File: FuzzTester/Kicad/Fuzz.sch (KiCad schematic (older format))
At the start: 8 parts, among them J1 Audio In/Out JST XH, J2 POT B10K JST XH, J3 POT B5K JST XH, J4 VOL POT A100K JST XH

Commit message: PCB fixes
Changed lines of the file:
@@
 encoding utf-8
 Sheet 1 10
-Title ""
+Title "Guitar Pedal Effect Fuzz Digitally Controlled"
 Date ""
-Rev ""
+Rev "0.1"
 Comp ""
 Comment1 ""
@@
 U 1 1 5EC42733
 P 5600 2200
-F 0 "R2" V 5393 2200 50  0000 C CNN
-F 1 "100K" V 5484 2200 50  0000 C CNN
+F 0 "R2" V 5500 2200 50  0000 C CNN
+F 1 "100K" V 5600 2200 50  0000 C CNN
 F 2 "Resistor_SMD:R_0805_2012Metric_Pad1.15x1.40mm_HandSolder" V 5530 2200 50  0001 C CNN
 F 3 "~" H 5600 2200 50  0001 C CNN
@@
 P 8400 1450
 F 0 "R3" H 8470 1496 50  0000 L CNN
-F 1 "10K" H 8470 1405 50  0000 L CNN
+F 1 "10K" H 8450 1400 50  0000 L CNN
 F 2 "Resistor_SMD:R_0805_2012Metric_Pad1.15x1.40mm_HandSolder" V 8330 1450 50  0001 C CNN
 F 3 "~" H 8400 1450 50  0001 C CNN

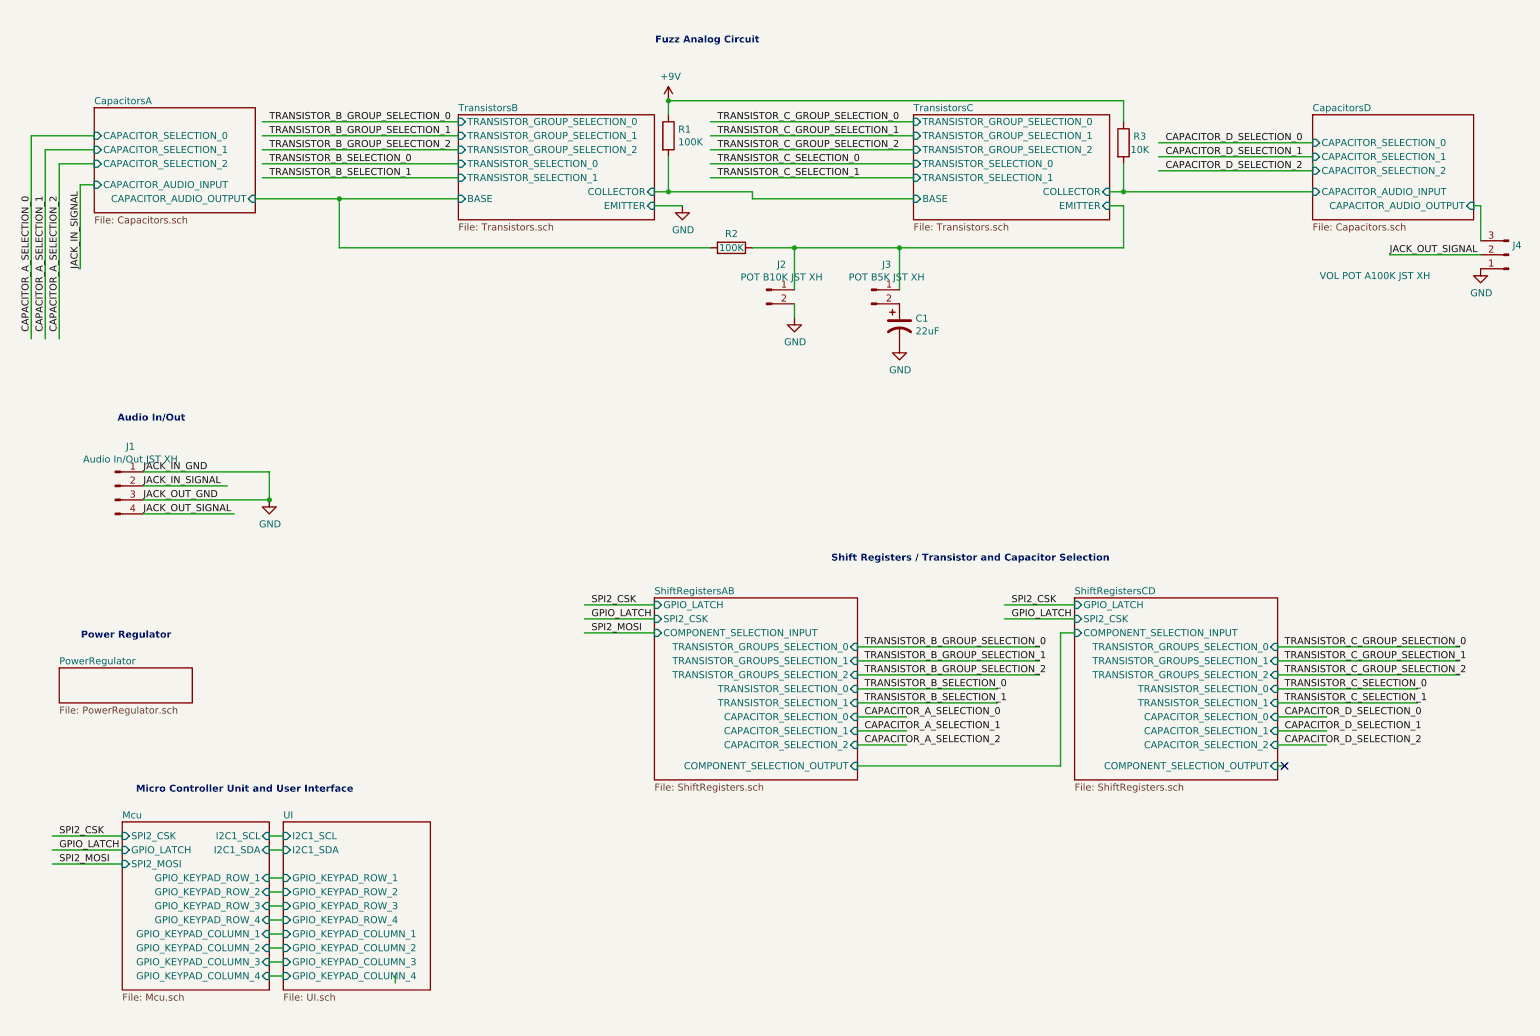
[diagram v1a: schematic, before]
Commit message: Schematics UI/MCU -> MCU + PCB improvements
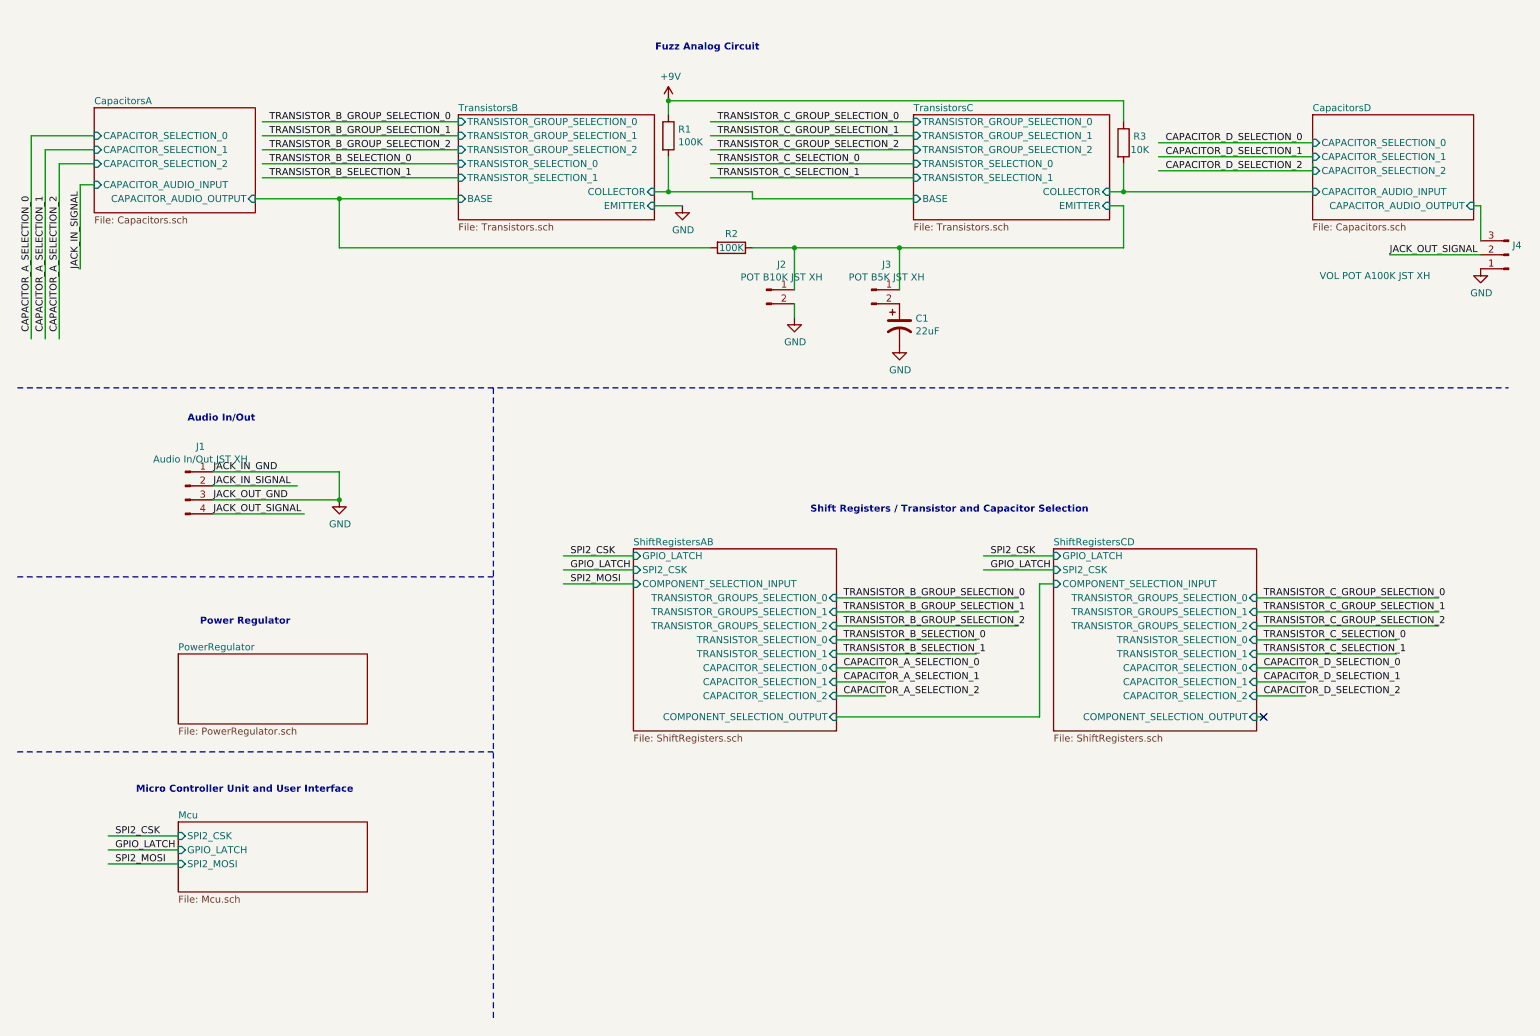
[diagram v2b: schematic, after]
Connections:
- wire segments 93 -> 82
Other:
- moved on the sheet: J1

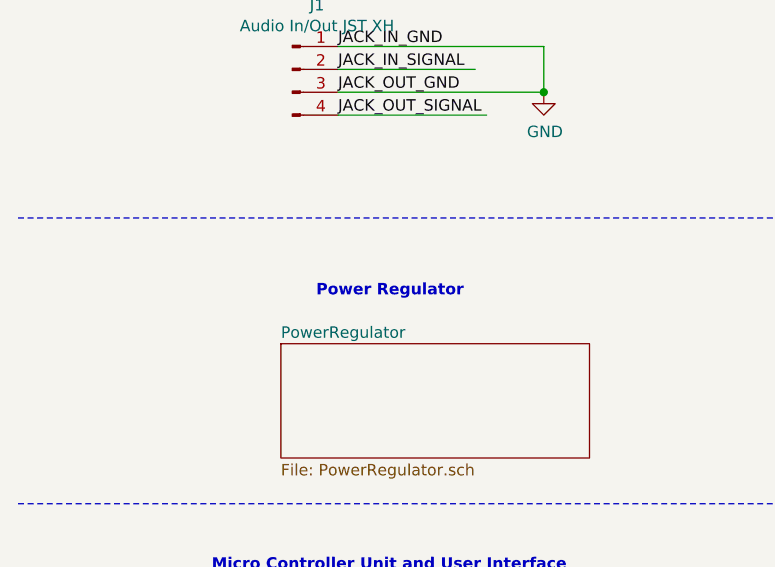
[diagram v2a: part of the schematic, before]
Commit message: Power regulator -9V
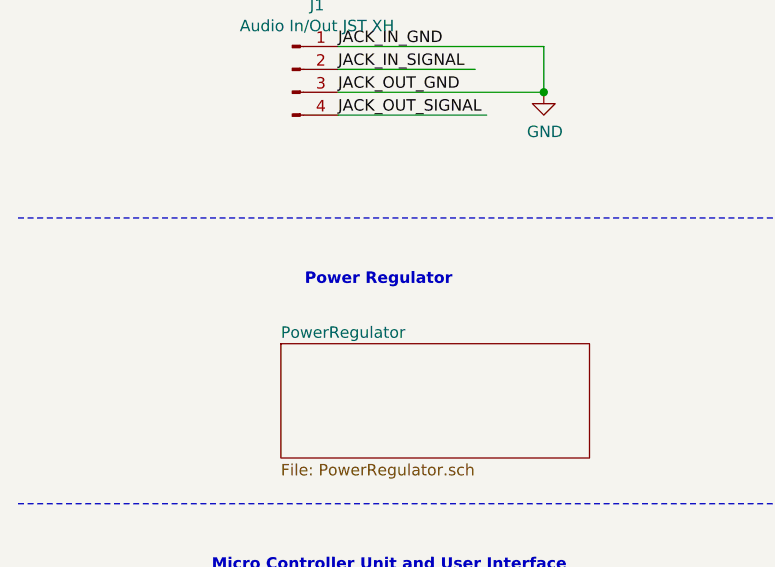
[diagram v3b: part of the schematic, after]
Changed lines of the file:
@@
 Text Notes 8150 4100 2    50   ~ 10
 Shift Registers / Transistor and Capacitor Selection\n
-Text Notes 2450 4900 2    50   ~ 10
+Text Notes 2400 4850 2    50   ~ 10
 Power Regulator\n
 Text Notes 2900 6100 2    50   ~ 10

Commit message: PCB Placement 100x82
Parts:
- removed J1: Audio In/Out JST XH, Connector_JST:JST_XH_B4B-XH-A_1x04_P2.50mm_Vertical, symbol Connector:Conn_01x04_Male
- added H1, H2, H3, H4: MountingHole, MountingHole:MountingHole_3.2mm_M3, symbol Mechanical:MountingHole
- C1: footprint Capacitor_SMD:C_0805_2012Metric_Pad1.15x1.40mm_HandSolder -> Capacitor_THT:CP_Radial_D5.0mm_P2.50mm
- R1, R2, R3: footprint Resistor_SMD:R_0805_2012Metric_Pad1.15x1.40mm_HandSolder -> Resistor_SMD:R_1206_3216Metric_Pad1.42x1.75mm_HandSolder
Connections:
- net labels added: 1602_BACK_LIGHT_PIN_1, 1602_BACK_LIGHT_PIN_2, BYPASS_MODE, BYPASS_MODE_3V3, CAPACITOR_A_SELECTION_3V3_0, CAPACITOR_A_SELECTION_3V3_1, CAPACITOR_A_SELECTION_3V3_2, CAPACITOR_D_SELECTION_3V3_0, CAPACITOR_D_SELECTION_3V3_1, CAPACITOR_D_SELECTION_3V3_2, JACK_IN_SIGNAL_THROUGH_FUZZ, JACK_OUT_SIGNAL_FROM_FUZZ, TRANSISTOR_B_GROUP_SELECTION_3V3_0, TRANSISTOR_B_GROUP_SELECTION_3V3_1, TRANSISTOR_B_GROUP_SELECTION_3V3_2, TRANSISTOR_B_SELECTION_3V3_0, TRANSISTOR_B_SELECTION_3V3_1, TRANSISTOR_C_GROUP_SELECTION_3V3_0, TRANSISTOR_C_GROUP_SELECTION_3V3_1, TRANSISTOR_C_GROUP_SELECTION_3V3_2, TRANSISTOR_C_SELECTION_3V3_0, TRANSISTOR_C_SELECTION_3V3_1
- net labels removed: JACK_IN_GND, JACK_IN_SIGNAL, JACK_OUT_GND, JACK_OUT_SIGNAL
- wire segments 82 -> 120
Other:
- note added: "Audio In/Out and Bypass\n\n"
- note added: "Mounting Holes\n\n"
- note removed: "Audio In/Out\n"
- moved on the sheet: C1, J2, J3, J4, R1, R2, R3

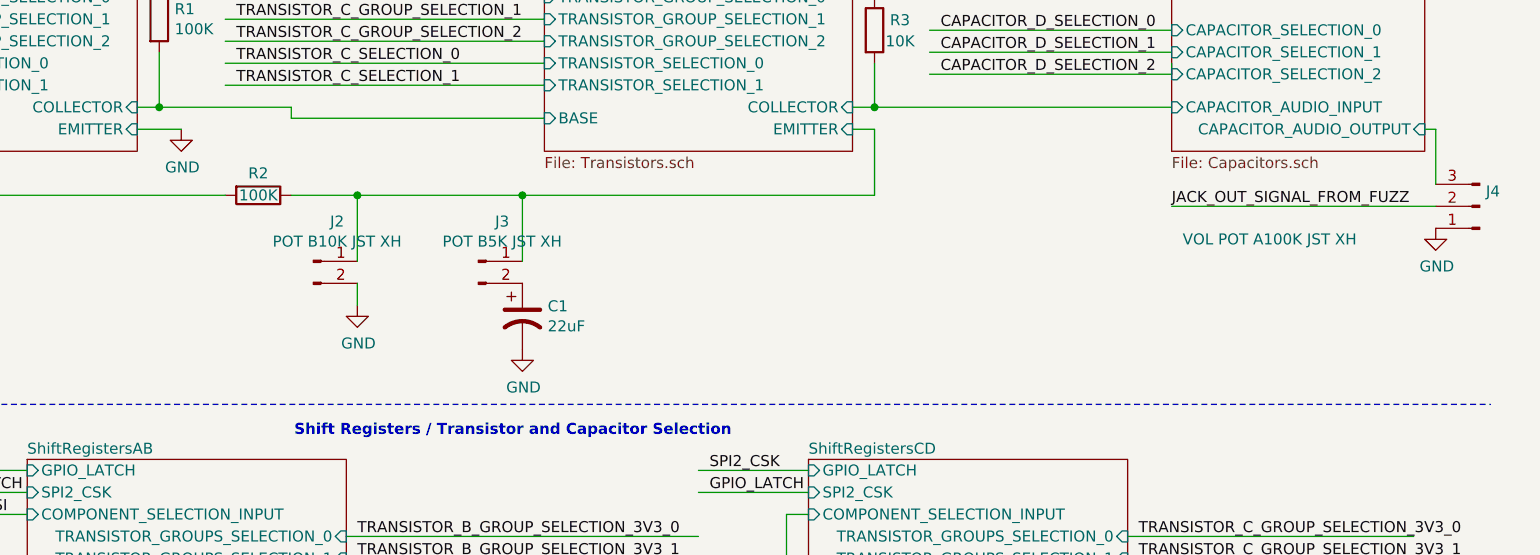
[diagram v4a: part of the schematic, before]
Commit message: GNDA, PCB DRC fixed
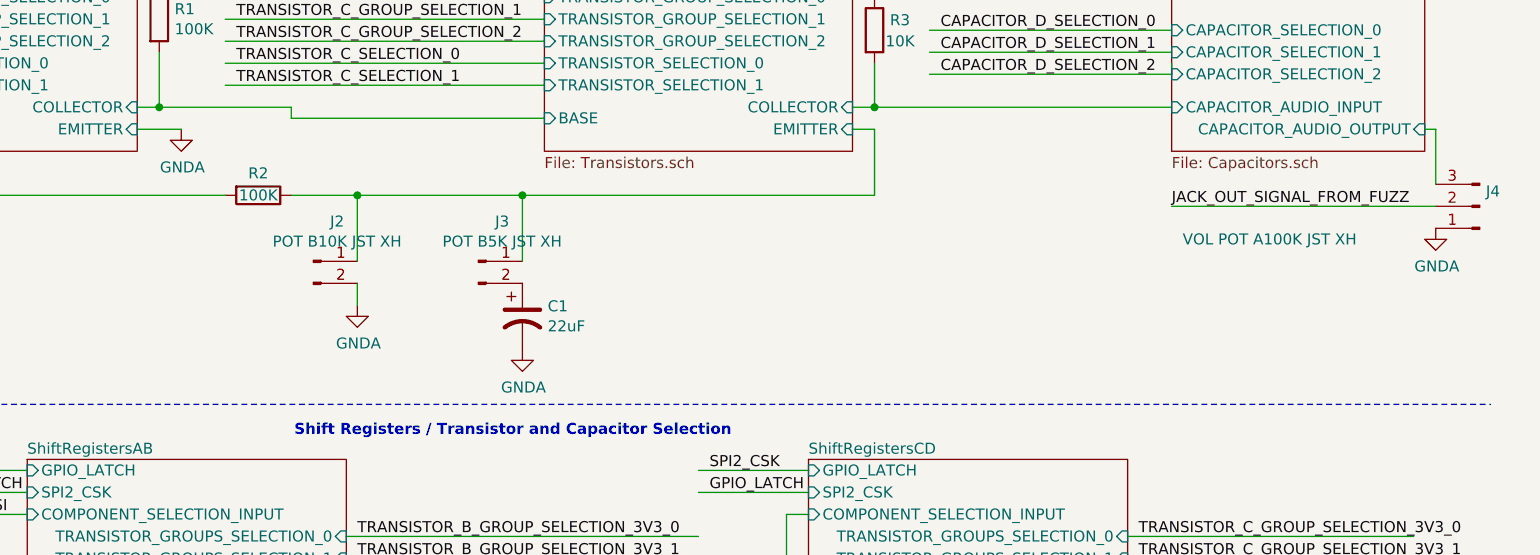
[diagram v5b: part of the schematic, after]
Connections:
- net labels added: GNDA
- net labels removed: GND
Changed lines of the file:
@@
-	1    0    0    -1
-$EndComp
-$Comp
-L power:GND #PWR03
-U 1 1 5F311D10
-P 6000 2500
-F 0 "#PWR03" H 6000 2250 50  0001 C CNN
-F 1 "GND" H 6005 2327 50  0000 C CNN
-F 2 "" H 6000 2500 50  0001 C CNN
-F 3 "" H 6000 2500 50  0001 C CNN
-	1    6000 2500
 	1    0    0    -1
 $EndComp
@@
 F 3 "~" H 6750 2550 50  0001 C CNN
 	1    6750 2550
-	1    0    0    -1
-$EndComp
-$Comp
-L power:GND #PWR02
-U 1 1 5F322620
-P 5200 1700
-F 0 "#PWR02" H 5200 1450 50  0001 C CNN
-F 1 "GND" H 5205 1527 50  0000 C CNN
-F 2 "" H 5200 1700 50  0001 C CNN
-F 3 "" H 5200 1700 50  0001 C CNN
-	1    5200 1700
 	1    0    0    -1
 $EndComp
@@
 	1    11100 2050
 	-1   0    0    1
-$EndComp
-$Comp
-L power:GND #PWR05
-U 1 1 5FA459A3
-P 10900 2150
-F 0 "#PWR05" H 10900 1900 50  0001 C CNN
-F 1 "GND" H 10905 1977 50  0000 C CNN
-F 2 "" H 10900 2150 50  0001 C CNN
-F 3 "" H 10900 2150 50  0001 C CNN
-	1    10900 2150
-	1    0    0    -1
-$EndComp
-$Comp
-L power:GND #PWR04
-U 1 1 5FA4B94D
-P 6750 2700
-F 0 "#PWR04" H 6750 2450 50  0001 C CNN
-F 1 "GND" H 6755 2527 50  0000 C CNN
-F 2 "" H 6750 2700 50  0001 C CNN
-F 3 "" H 6750 2700 50  0001 C CNN
-	1    6750 2700
-	1    0    0    -1
 $EndComp
 Wire Wire Line
@@
 F7 "BYPASS_MODE_3V3" I L 1650 6750 50
 $EndSheet
+$Comp
+L power:GNDA #PWR03
+U 1 1 5EA13AD0
+P 6000 2500
+F 0 "#PWR03" H 6000 2250 50  0001 C CNN
+F 1 "GNDA" H 6005 2327 50  0000 C CNN
+F 2 "" H 6000 2500 50  0001 C CNN
+F 3 "" H 6000 2500 50  0001 C CNN
+	1    6000 2500
+	1    0    0    -1
+$EndComp
+$Comp
+L power:GNDA #PWR04
+U 1 1 5EA14305
+P 6750 2700
+F 0 "#PWR04" H 6750 2450 50  0001 C CNN
+F 1 "GNDA" H 6755 2527 50  0000 C CNN
+F 2 "" H 6750 2700 50  0001 C CNN
+F 3 "" H 6750 2700 50  0001 C CNN
+	1    6750 2700
+	1    0    0    -1
+$EndComp
+$Comp
+L power:GNDA #PWR05
+U 1 1 5EA148BB
+P 10900 2150
+F 0 "#PWR05" H 10900 1900 50  0001 C CNN
+F 1 "GNDA" H 10905 1977 50  0000 C CNN
+F 2 "" H 10900 2150 50  0001 C CNN
+F 3 "" H 10900 2150 50  0001 C CNN
+	1    10900 2150
+	1    0    0    -1
+$EndComp
+$Comp
+L power:GNDA #PWR02
+U 1 1 5EA15848
+P 5200 1700
+F 0 "#PWR02" H 5200 1450 50  0001 C CNN
+F 1 "GNDA" H 5205 1527 50  0000 C CNN
+F 2 "" H 5200 1700 50  0001 C CNN
+F 3 "" H 5200 1700 50  0001 C CNN
+	1    5200 1700
+	1    0    0    -1
+$EndComp
 $EndSCHEMATC
